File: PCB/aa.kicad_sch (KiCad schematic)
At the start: 11 parts, among them J9 Amp, U3 LM386

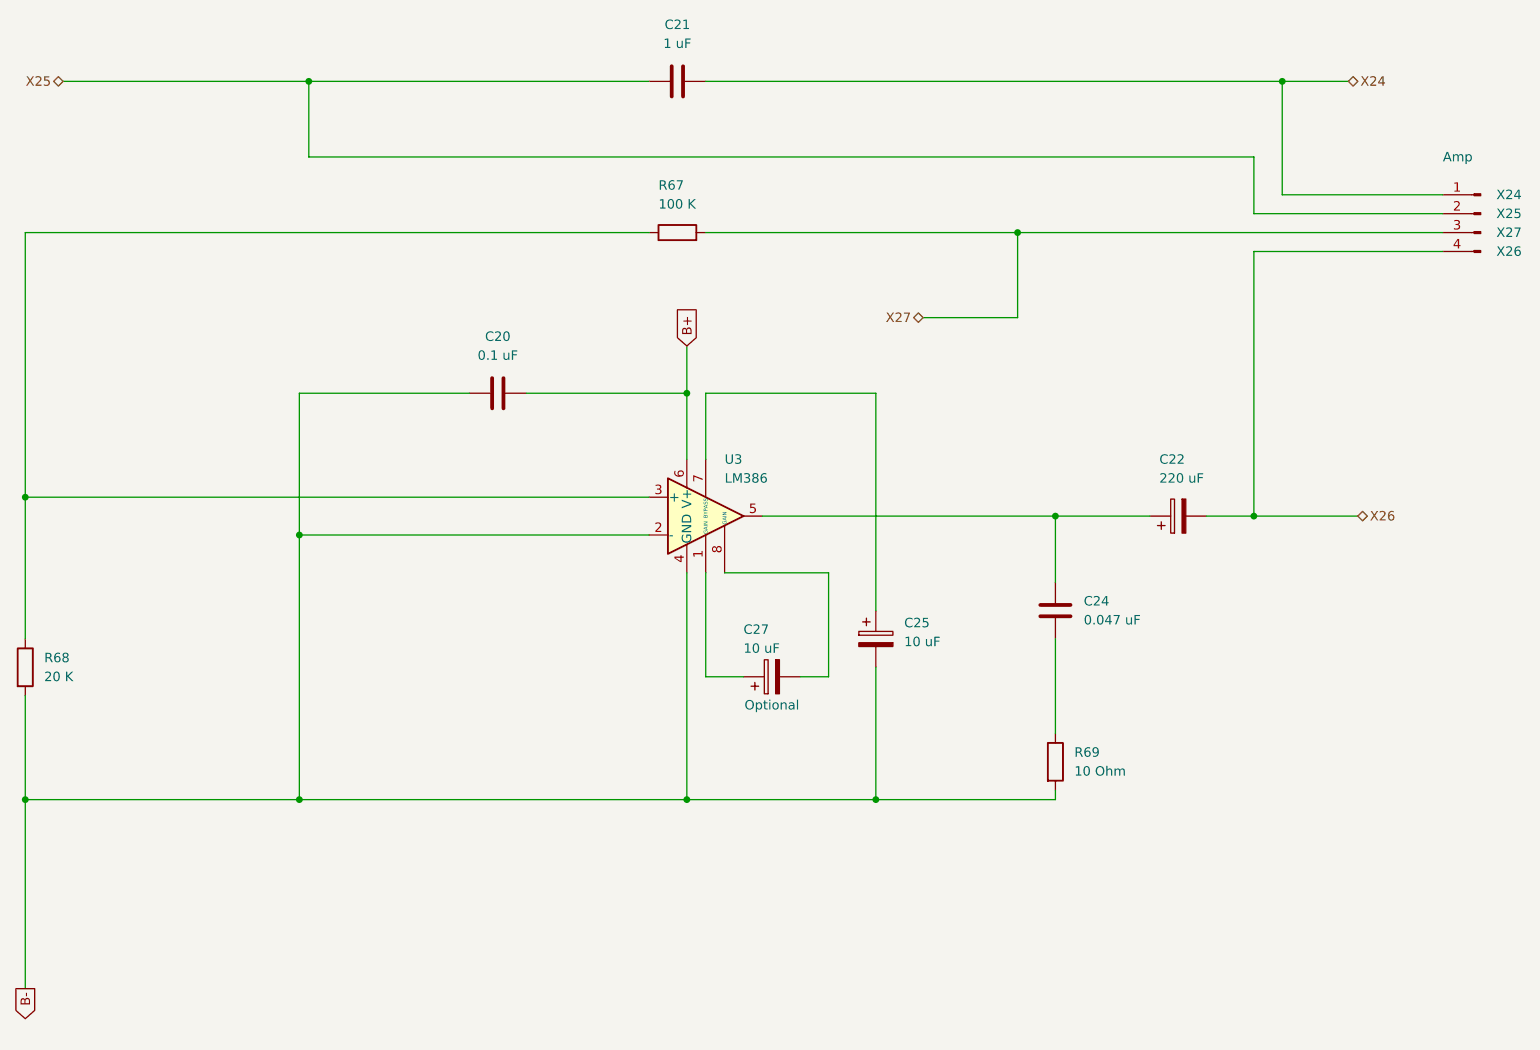
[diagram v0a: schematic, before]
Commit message: Change TO-92 transistors to wide package to avoid shorting during soldering
Added B- hole for speaker
Added more vias to shorten traces
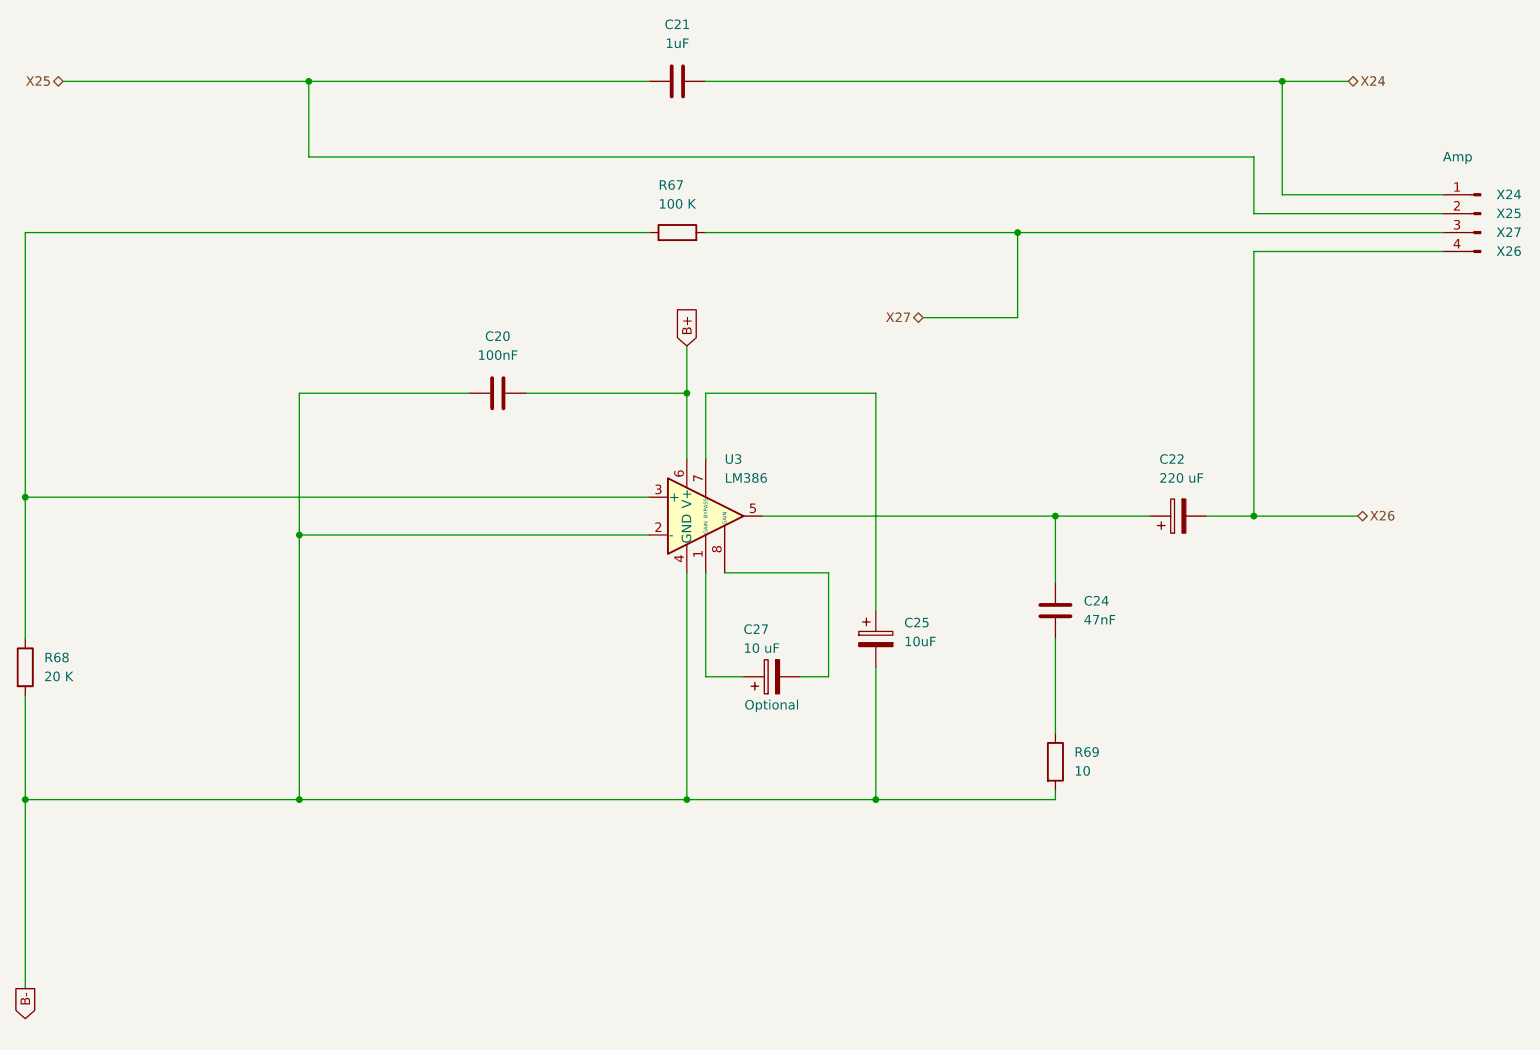
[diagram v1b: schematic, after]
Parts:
- C20: value 0.1 uF -> 100nF
- C21: value 1 uF -> 1uF
- C24: value 0.047 uF -> 47nF
- C25: value 10 uF -> 10uF
- R69: value 10 Ohm -> 10
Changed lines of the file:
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@@
 		(fields_autoplaced yes)
 		(property "Reference" "R69"
-			(at 191.77 134.62 0)
+			(at 191.77 134.6199 0)
 			(show_name no)
 			(do_not_autoplace no)
@@
 			)
 		)
-		(property "Value" "10 Ohm"
-			(at 191.77 137.16 0)
+		(property "Value" "10"
+			(at 191.77 137.1599 0)
 			(show_name no)
 			(do_not_autoplace no)
@@
 		(fields_autoplaced yes)
 		(property "Reference" "C24"
-			(at 193.04 114.3 0)
+			(at 193.04 114.2999 0)
 			(show_name no)
 			(do_not_autoplace no)
@@
 			)
 		)
-		(property "Value" "0.047 uF"
-			(at 193.04 116.84 0)
+		(property "Value" "47nF"
+			(at 193.04 116.8399 0)
 			(show_name no)
 			(do_not_autoplace no)
@@
 			)
 		)
-		(property "Value" "0.1 uF"
+		(property "Value" "100nF"
 			(at 114.3 81.28 90)
 			(show_name no)
@@
 		(fields_autoplaced yes)
 		(property "Reference" "C25"
-			(at 168.91 117.221 0)
+			(at 168.91 117.2209 0)
 			(show_name no)
 			(do_not_autoplace no)
@@
 			)
 		)
-		(property "Value" "10 uF"
-			(at 168.91 119.761 0)
+		(property "Value" "10uF"
+			(at 168.91 119.7609 0)
 			(show_name no)
 			(do_not_autoplace no)
@@
 			)
 		)
-		(property "Value" "1 uF"
+		(property "Value" "1uF"
 			(at 138.43 39.37 90)
 			(show_name no)

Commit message: Necessary Changes to Schematic and PCB
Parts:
- removed J9: Amp, Connector_PinHeader_2.00mm:PinHeader_1x04_P2.00mm_Vertical, symbol Connector:Conn_01x04_Pin
- added J9: Amp, Connector_PinSocket_2.54mm:PinSocket_1x05_P2.54mm_Vertical, symbol Connector:Conn_01x05_Pin
- C25: footprint Capacitor_THT:CP_Radial_D4.0mm_P1.50mm -> Capacitor_THT:CP_Radial_D4.0mm_P2.00mm
- C27: footprint Capacitor_THT:CP_Radial_D4.0mm_P1.50mm -> Capacitor_THT:CP_Radial_D4.0mm_P2.00mm; symbol Device:C_Polarized -> Device:C
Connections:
- net B-: now also J9.5 (Pin_5)
- net X24: now also J9.1 (Pin_1)
- net X25: now also J9.2 (Pin_2)
- net X26: now also J9.4 (Pin_4)
- net X27: now also J9.3 (Pin_3)
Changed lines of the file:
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@@
+	(wire
+		(pts
+			(xy 228.6 69.85) (xy 241.3 69.85)
+		)
+		(stroke
+			(width 0)
+			(type default)
+		)
+	)
 	(wire
 		(pts
@@
 			(width 0)
 			(type default)
+		)
+	)
+	(global_label "B-"
+		(shape output)
+		(at 228.6 69.85 180)
+		(fields_autoplaced yes)
+		(effects
+			(font
+				(size 1.27 1.27)
+			)
+			(justify right)
+		)
+		(property "Intersheetrefs" "${INTERSHEET_REFS}"
+			(at 222.7724 69.85 0)
+			(hide yes)
+			(show_name no)
+			(do_not_autoplace no)
+			(effects
+				(font
+					(size 1.27 1.27)
+				)
+				(justify right)
+			)
 		)
 	)
@@
 	)
 	(symbol
-		(lib_id "Connector:Conn_01x04_Pin")
-		(at 246.38 62.23 0)
-		(mirror y)
-		(unit 1)
-		(body_style 1)
-		(exclude_from_sim no)
-		(in_bom yes)
-		(on_board yes)
-		(in_pos_files yes)
-		(dnp no)
-		(property "Reference" "J9"
-			(at 247.65 64.77 0)
-			(hide yes)
-			(show_name no)
-			(do_not_autoplace no)
-			(effects
-				(font
-					(size 1.27 1.27)
-				)
-				(justify right)
-			)
-		)
-		(property "Value" "Amp"
-			(at 241.3 54.61 0)
-			(show_name no)
-			(do_not_autoplace no)
-			(effects
-				(font
-					(size 1.27 1.27)
-				)
-				(justify right)
-			)
-		)
-		(property "Footprint" "Connector_PinHeader_2.00mm:PinHeader_1x04_P2.00mm_Vertical"
-			(at 246.38 62.23 0)
-			(hide yes)
-			(show_name no)
-			(do_not_autoplace no)
-			(effects
-				(font
-					(size 1.27 1.27)
-				)
-			)
-		)
-		(property "Datasheet" ""
-			(at 246.38 62.23 0)
-			(hide yes)
-			(show_name no)
-			(do_not_autoplace no)
-			(effects
-				(font
-					(size 1.27 1.27)
-				)
-			)
-		)
-		(property "Description" ""
-			(at 246.38 62.23 0)
-			(hide yes)
-			(show_name no)
-			(do_not_autoplace no)
-			(effects
-				(font
-					(size 1.27 1.27)
-				)
-			)
-		)
-		(property "X24" "X24"
-			(at 250.19 59.69 0)
-			(show_name no)
-			(do_not_autoplace no)
-			(effects
-				(font
-					(size 1.27 1.27)
-				)
-			)
-		)
-		(property "X25" "X25"
-			(at 250.19 62.23 0)
-			(show_name no)
-			(do_not_autoplace no)
-			(effects
-				(font
-					(size 1.27 1.27)
-				)
-			)
-		)
-		(property "X27" "X27"
-			(at 250.19 64.77 0)
-			(show_name no)
-			(do_not_autoplace no)
-			(effects
-				(font
-					(size 1.27 1.27)
-				)
-			)
-		)
-		(property "X26" "X26"
-			(at 250.19 67.31 0)
-			(show_name no)
-			(do_not_autoplace no)
-			(effects
-				(font
-					(size 1.27 1.27)
-				)
-			)
-		)
-		(pin "1"
-		)
-		(pin "2"
-		)
-		(pin "3"
-		)
-		(pin "4"
-		)
-		(instances
-			(project "Noise Toaster PCB"
-				(path "/7be3f398-d902-4566-9ee4-0bff072cd47e/8b7babf3-8af2-4de0-abdc-510e7f40fd33"
-					(reference "J9")
-					(unit 1)
-				)
-			)
-		)
-	)
-	(symbol
 		(lib_id "Device:C")
 		(at 189.23 115.57 0)
@@
 			)
 		)
-		(property "Footprint" "Capacitor_THT:CP_Radial_D4.0mm_P1.50mm"
+		(property "Footprint" "Capacitor_THT:CP_Radial_D4.0mm_P2.00mm"
 			(at 166.0652 123.19 0)
 			(hide yes)
@@
 				(path "/7be3f398-d902-4566-9ee4-0bff072cd47e/8b7babf3-8af2-4de0-abdc-510e7f40fd33"
 					(reference "C25")
+					(unit 1)
+				)
+			)
+		)
+	)
+	(symbol
+		(lib_id "Connector:Conn_01x05_Pin")
+		(at 246.38 64.77 0)
+		(mirror y)
+		(unit 1)
+		(body_style 1)
+		(exclude_from_sim no)
+		(in_bom yes)
+		(on_board yes)
+		(in_pos_files yes)
+		(dnp no)
+		(property "Reference" "J9"
+			(at 247.65 67.31 0)
+			(hide yes)
+			(show_name no)
+			(do_not_autoplace no)
+			(effects
+				(font
+					(size 1.27 1.27)
+				)
+				(justify right)
+			)
+		)
+		(property "Value" "Amp"
+			(at 241.3 57.15 0)
+			(show_name no)
+			(do_not_autoplace no)
+			(effects
+				(font
+					(size 1.27 1.27)
+				)
+				(justify right)
+			)
+		)
+		(property "Footprint" "Connector_PinSocket_2.54mm:PinSocket_1x05_P2.54mm_Vertical"
+			(at 246.38 64.77 0)
+			(hide yes)
+			(show_name no)
+			(do_not_autoplace no)
+			(effects
+				(font
+					(size 1.27 1.27)
+				)
+			)
+		)
+		(property "Datasheet" ""
+			(at 246.38 64.77 0)
+			(hide yes)
+			(show_name no)
+			(do_not_autoplace no)
+			(effects
+				(font
+					(size 1.27 1.27)
+				)
+			)
+		)
+		(property "Description" "Generic connector, single row, 01x05, script generated"
+			(at 246.38 64.77 0)
+			(hide yes)
+			(show_name no)
+			(do_not_autoplace no)
+			(effects
+				(font
+					(size 1.27 1.27)
+				)
+			)
+		)
+		(property "X24" "X24"
+			(at 250.19 59.69 0)
+			(show_name no)
+			(do_not_autoplace no)
+			(effects
+				(font
+					(size 1.27 1.27)
+				)
+			)
+		)
+		(property "X25" "X25"
+			(at 250.19 62.23 0)
+			(show_name no)
+			(do_not_autoplace no)
+			(effects
+				(font
+					(size 1.27 1.27)
+				)
+			)
+		)
+		(property "X27" "X27"
+			(at 250.19 64.77 0)
+			(show_name no)
+			(do_not_autoplace no)
+			(effects
+				(font
+					(size 1.27 1.27)
+				)
+			)
+		)
+		(property "X26" "X26"
+			(at 250.19 67.31 0)
+			(show_name no)
+			(do_not_autoplace no)
+			(effects
+				(font
+					(size 1.27 1.27)
+				)
+			)
+		)
+		(property "B-" "B-"
+			(at 249.682 69.85 0)
+			(show_name no)
+			(do_not_autoplace no)
+			(effects
+				(font
+					(size 1.27 1.27)
+				)
+			)
+		)
+		(pin "1"
+		)
+		(pin "2"
+		)
+		(pin "3"
+		)
+		(pin "4"
+		)
+		(pin "5"
+		)
+		(instances
+			(project "Noise Toaster PCB"
+				(path "/7be3f398-d902-4566-9ee4-0bff072cd47e/8b7babf3-8af2-4de0-abdc-510e7f40fd33"
+					(reference "J9")
 					(unit 1)
 				)
@@
 	)
 	(symbol
-		(lib_id "Device:C_Polarized")
+		(lib_id "Device:C")
 		(at 151.13 124.46 90)
 		(unit 1)
@@
 			)
 		)
-		(property "Footprint" "Capacitor_THT:CP_Radial_D4.0mm_P1.50mm"
+		(property "Footprint" "Capacitor_THT:CP_Radial_D4.0mm_P2.00mm"
 			(at 154.94 123.4948 0)
 			(hide yes)
@@
 			)
 		)
-		(property "Description" ""
+		(property "Description" "Unpolarized capacitor"
 			(at 151.13 124.46 0)
 			(hide yes)

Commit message: Fixed grave mistake (Q10 position swapped)
Tom forgot to mirror Q10, swapping the emitter and collectors of Q10
Changed all the footprints of electrolytic caps to 5mm (i didnt find a single cap in my parts bin rated for 25V that was 4mm diameter)
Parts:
- C25, C27: footprint Capacitor_THT:CP_Radial_D4.0mm_P2.00mm -> Capacitor_THT:CP_Radial_D5.0mm_P2.00mm
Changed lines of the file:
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@@
 			)
 		)
-		(property "Footprint" "Capacitor_THT:CP_Radial_D4.0mm_P2.00mm"
+		(property "Footprint" "Capacitor_THT:CP_Radial_D5.0mm_P2.00mm"
 			(at 166.0652 123.19 0)
 			(hide yes)
@@
 			)
 		)
-		(property "Footprint" "Capacitor_THT:CP_Radial_D4.0mm_P2.00mm"
+		(property "Footprint" "Capacitor_THT:CP_Radial_D5.0mm_P2.00mm"
 			(at 154.94 123.4948 0)
 			(hide yes)

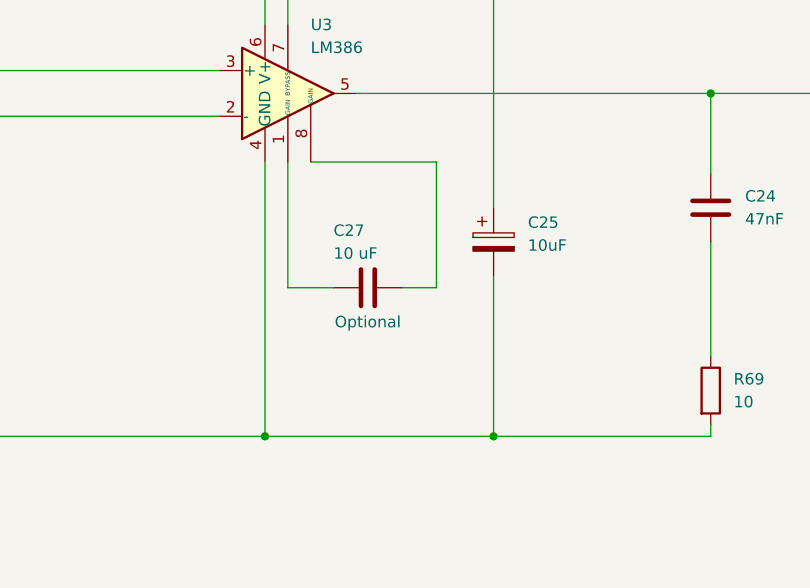
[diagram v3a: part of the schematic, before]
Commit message: Final Update
Move power pins closer to filter caps
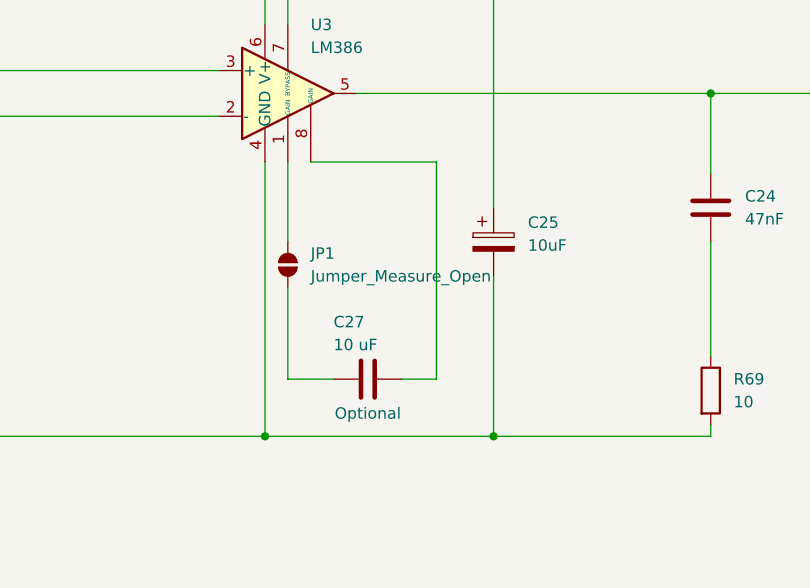
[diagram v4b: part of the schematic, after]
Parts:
- added JP1: Jumper_Measure_Open, PCM_SparkFun-Jumper:Jumper_2_PTH_SMD_Combo-NO, symbol PCM_SparkFun-Jumper:Jumper_Measure_Open
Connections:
- net at U3.1 (GAIN): now also JP1.2 (B); no longer C27.1
- new net: C27.1, JP1.1 (A)
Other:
- moved on the sheet: C27
